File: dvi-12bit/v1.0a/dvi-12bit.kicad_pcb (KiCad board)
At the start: 4 copper layers, 40 x 40.8 mm, 33 parts, among them J1 PMOD, J2 PMOD, J3 jmp, J4 5V, J5 jmp, J6 HDMI_A_1.4, U1 VREG_3V3, U2 TFP410

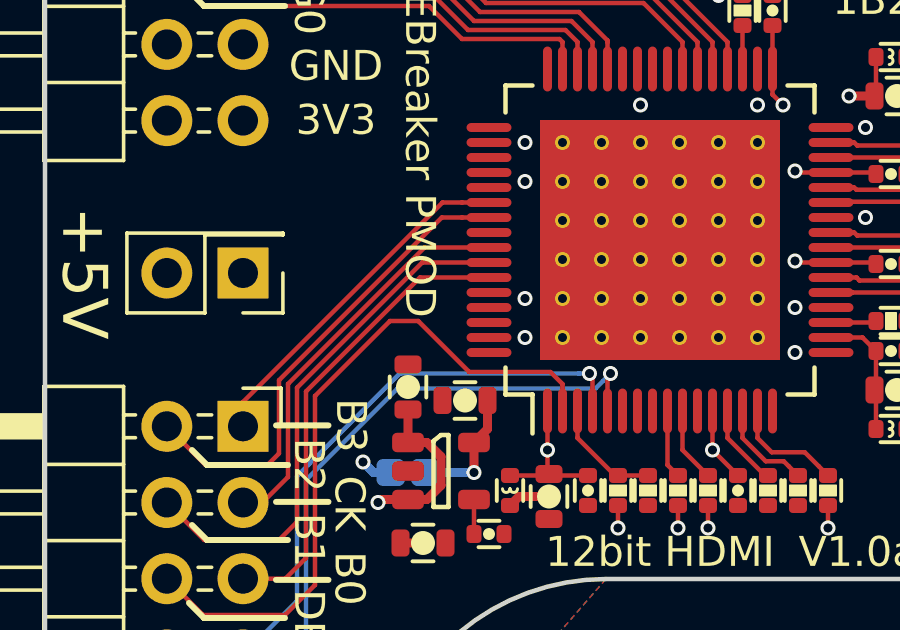
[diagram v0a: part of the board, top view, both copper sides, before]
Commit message: Added some more GND via.
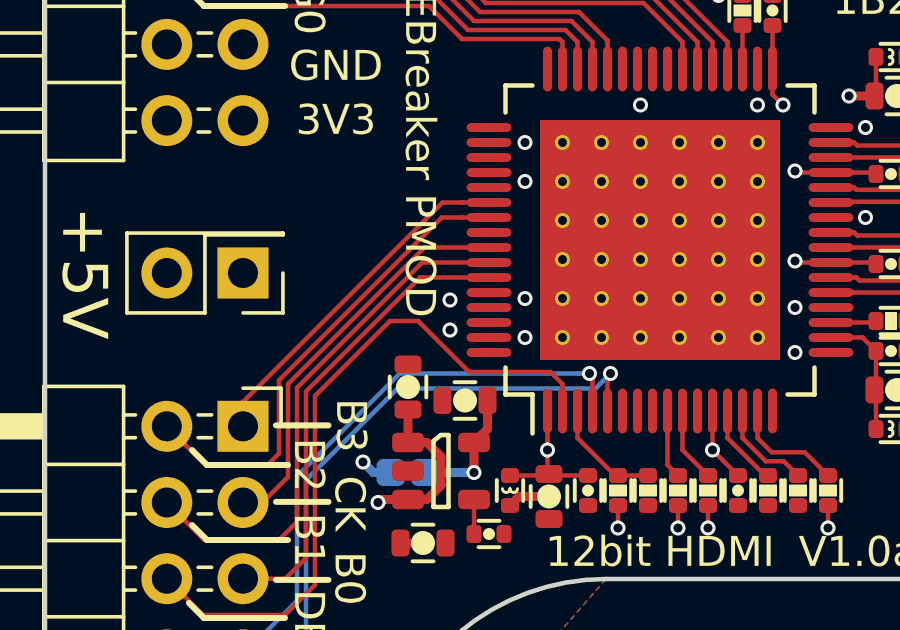
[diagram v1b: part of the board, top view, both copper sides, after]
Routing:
- net GND: vias 24 -> 26
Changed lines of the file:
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@@
     (thickness 1.6)
     (drawings 114)
-    (tracks 316)
+    (tracks 318)
     (zones 0)
     (modules 33)
@@
   (via (at 59.85 34.3) (size 0.5) (drill 0.3) (layers F.Cu B.Cu) (net 1))
   (via (at 59.4 38.35) (size 0.5) (drill 0.3) (layers F.Cu B.Cu) (net 1))
+  (via (at 43.5 41.1) (size 0.5) (drill 0.3) (layers F.Cu B.Cu) (net 1))
+  (via (at 43.5 42.1) (size 0.5) (drill 0.3) (layers F.Cu B.Cu) (net 1))
   (via (at 44.3 46.85) (size 0.5) (drill 0.3) (layers F.Cu B.Cu) (net 2))
   (segment (start 42.675 46.85) (end 44.3 46.85) (width 0.3) (layer B.Cu) (net 2))
@@
   (via (at 59.5 33) (size 0.5) (drill 0.3) (layers F.Cu B.Cu) (net 2))
   (segment (start 58.7 33) (end 59.5 33) (width 0.15) (layer F.Cu) (net 2))
-  (segment (start 59.6 46.875) (end 60.425 46.875) (width 0.3) (layer B.Cu) (net 34))
-  (via (at 63 44.3) (size 0.5) (drill 0.3) (layers F.Cu B.Cu) (net 34))
-  (segment (start 60.425 46.875) (end 63 44.3) (width 0.3) (layer B.Cu) (net 34))
-  (segment (start 62.65 43.95) (end 63 44.3) (width 0.15) (layer F.Cu) (net 34))
-  (segment (start 61.55 43.95) (end 62.65 43.95) (width 0.15) (layer F.Cu) (net 34))
   (segment (start 42.1 44.75) (end 42.1 45.849999) (width 0.3) (layer F.Cu) (net 3))
   (segment (start 42.73 45.849999) (end 43.2 46.319999) (width 0.3) (layer F.Cu) (net 3))
@@
   (segment (start 57.65 41.85) (end 57.7 41.8) (width 0.15) (layer F.Cu) (net 33))
   (segment (start 56.2 41.85) (end 57.65 41.85) (width 0.15) (layer F.Cu) (net 33))
+  (segment (start 59.6 46.875) (end 60.425 46.875) (width 0.3) (layer B.Cu) (net 34))
+  (via (at 63 44.3) (size 0.5) (drill 0.3) (layers F.Cu B.Cu) (net 34))
+  (segment (start 60.425 46.875) (end 63 44.3) (width 0.3) (layer B.Cu) (net 34))
+  (segment (start 62.65 43.95) (end 63 44.3) (width 0.15) (layer F.Cu) (net 34))
+  (segment (start 61.55 43.95) (end 62.65 43.95) (width 0.15) (layer F.Cu) (net 34))
   (segment (start 42.498556 40.35) (end 44.8 40.35) (width 0.15) (layer F.Cu) (net 35))
   (segment (start 38.7 44.148556) (end 42.498556 40.35) (width 0.15) (layer F.Cu) (net 35))

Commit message: Some global cleanup.
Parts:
- added REF**: null_Logo_SilkS_10mm, pkl_logos:null_Logo_SilkS_10mm, B.Cu at (49.4, 40.2)
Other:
- board text added: "NULL"
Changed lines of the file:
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@@
-(kicad_pcb (version 20171130) (host pcbnew 5.0.0-fee4fd1~66~ubuntu18.04.1)
+(kicad_pcb (version 20171130) (host pcbnew 5.1.5-52549c5~86~ubuntu19.10.1)
   (general
     (thickness 1.6)
-    (drawings 114)
+    (drawings 115)
     (tracks 318)
     (zones 0)
-    (modules 33)
+    (modules 34)
     (nets 52)
   )
@@
     (zone_45_only no)
     (trace_min 0.15)
-    (segment_width 0.2)
-    (edge_width 0.15)
     (via_size 0.5)
     (via_drill 0.3)
@@
     (uvia_min_size 0.2)
     (uvia_min_drill 0.1)
+    (edge_width 0.15)
+    (segment_width 0.2)
     (pcb_text_width 0.3)
     (pcb_text_size 1.5 1.5)
@@
     (add_net "Net-(U2-Pad8)")
   )
+  (module pkl_logos:null_Logo_SilkS_10mm (layer B.Cu)
+    (at 49.4 40.2 90)
+    (fp_text reference REF** (at 0 -6 90) (layer B.Fab)
+      (effects (font (size 1 1) (thickness 0.15)) (justify mirror))
+    )
+    (fp_text value null_Logo_SilkS_10mm (at 0 6.35 90) (layer B.Fab)
+      (effects (font (size 1 1) (thickness 0.15)) (justify mirror))
+    )
+    (fp_arc (start -0.4 -0.2) (end -0.7 -0.2) (angle 180) (layer B.SilkS) (width 0.15))
+    (fp_line (start 1 -0.5) (end 1.5 -0.5) (layer B.SilkS) (width 0.15))
+    (fp_line (start 1 0.5) (end 1 -0.5) (layer B.SilkS) (width 0.15))
+    (fp_line (start 0.2 -0.5) (end 0.7 -0.5) (layer B.SilkS) (width 0.15))
+    (fp_line (start 0.2 0.5) (end 0.2 -0.5) (layer B.SilkS) (width 0.15))
+    (fp_line (start -0.1 0.5) (end -0.1 -0.2) (layer B.SilkS) (width 0.15))
+    (fp_line (start -0.7 0.5) (end -0.7 -0.2) (layer B.SilkS) (width 0.15))
+    (fp_line (start -1 -0.5) (end -1 0.5) (layer B.SilkS) (width 0.15))
+    (fp_line (start -1.5 0.5) (end -1 -0.5) (layer B.SilkS) (width 0.15))
+    (fp_line (start -1.5 -0.5) (end -1.5 0.5) (layer B.SilkS) (width 0.15))
+    (fp_line (start 5 5) (end -5 5) (layer B.SilkS) (width 0.4))
+    (fp_line (start -5 5) (end -5 -5) (layer B.SilkS) (width 0.4))
+    (fp_line (start 5 5) (end 5 -5) (layer B.SilkS) (width 0.4))
+    (fp_line (start -5 -5) (end 5 -5) (layer B.SilkS) (width 0.4))
+  )
   (module pkl_connectors:PMODHeader_2x06_P2.54mm_Horizontal (layer F.Cu)
     (at 36.6 35.12 180)
@@
     )
   )
+  (gr_text NULL (at 42.8 40.2 270) (layer B.SilkS)
+    (effects (font (size 1 1) (thickness 0.2)) (justify mirror))
+  )
   (gr_text R3 (at 40.2 22.58 270) (layer B.SilkS)
